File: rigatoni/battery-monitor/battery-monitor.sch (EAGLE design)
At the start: 39 parts, among them J1 S2B-XH-A_(LF)(SN), J2 QSH-030-01-X-D-A-XX, J4 S4B-XH-A(LF)(SN), Q1 STT4P3LLH6, U1 LT1930ES5TRMPBF_BOOST_CONV, U2 NUCLEO-H743ZI-HEADER, U3 TPSM84205EAB

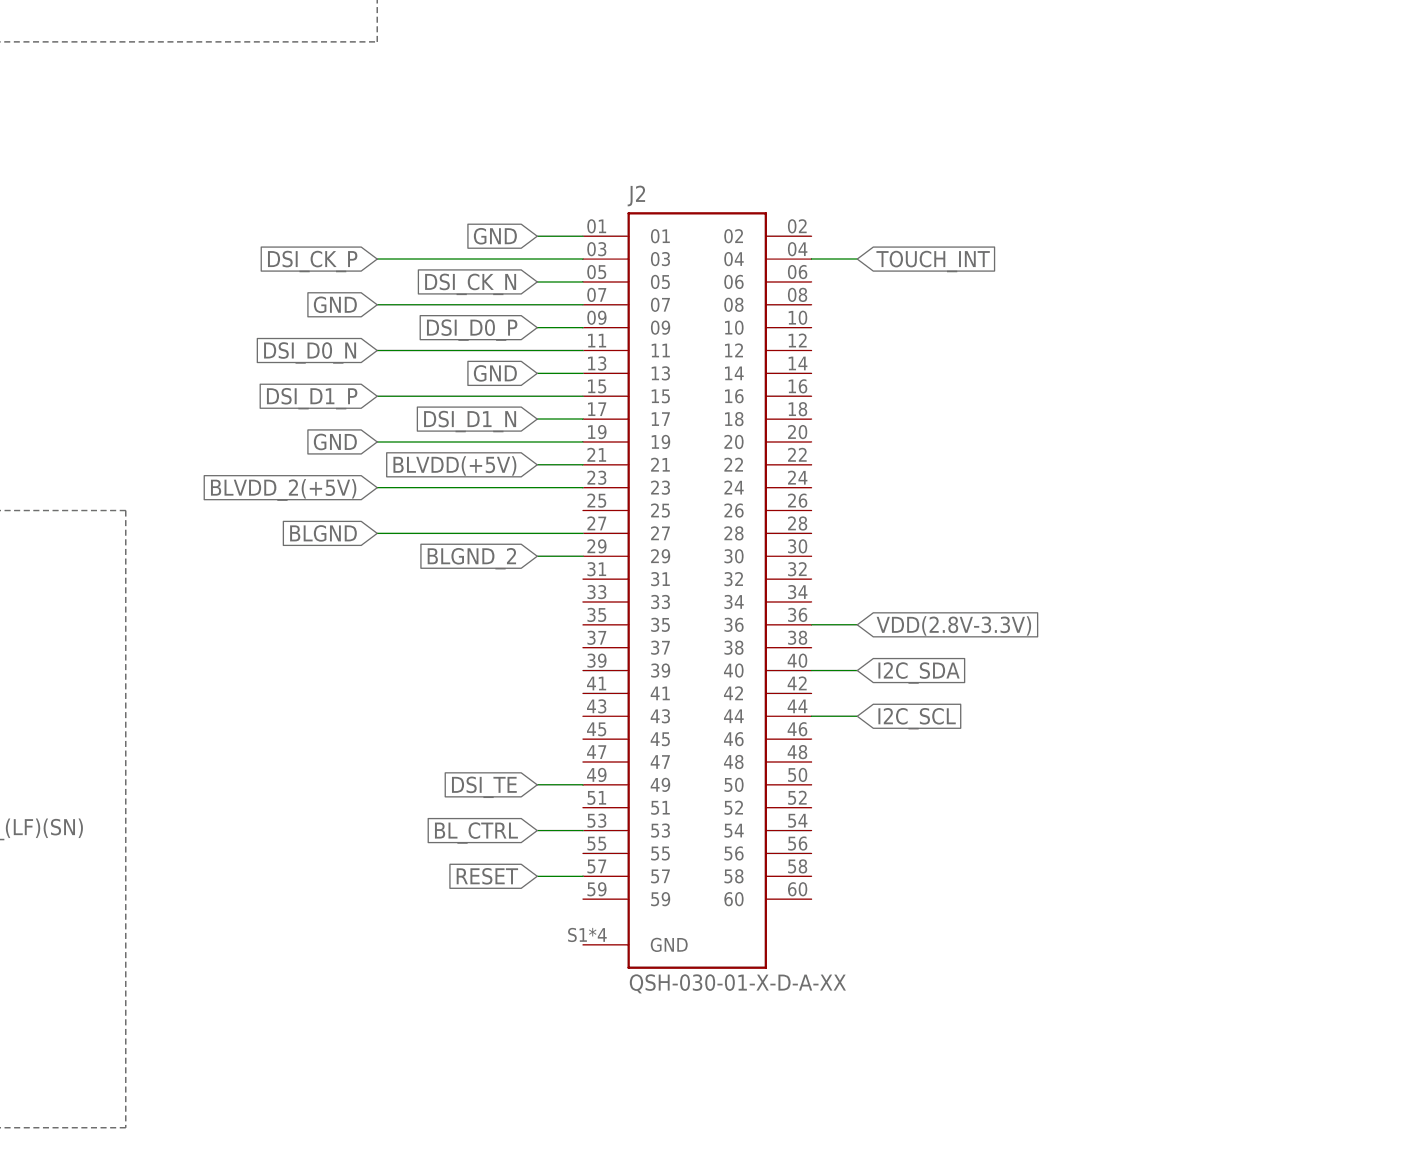
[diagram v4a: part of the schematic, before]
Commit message: Update battery-monitor.sch
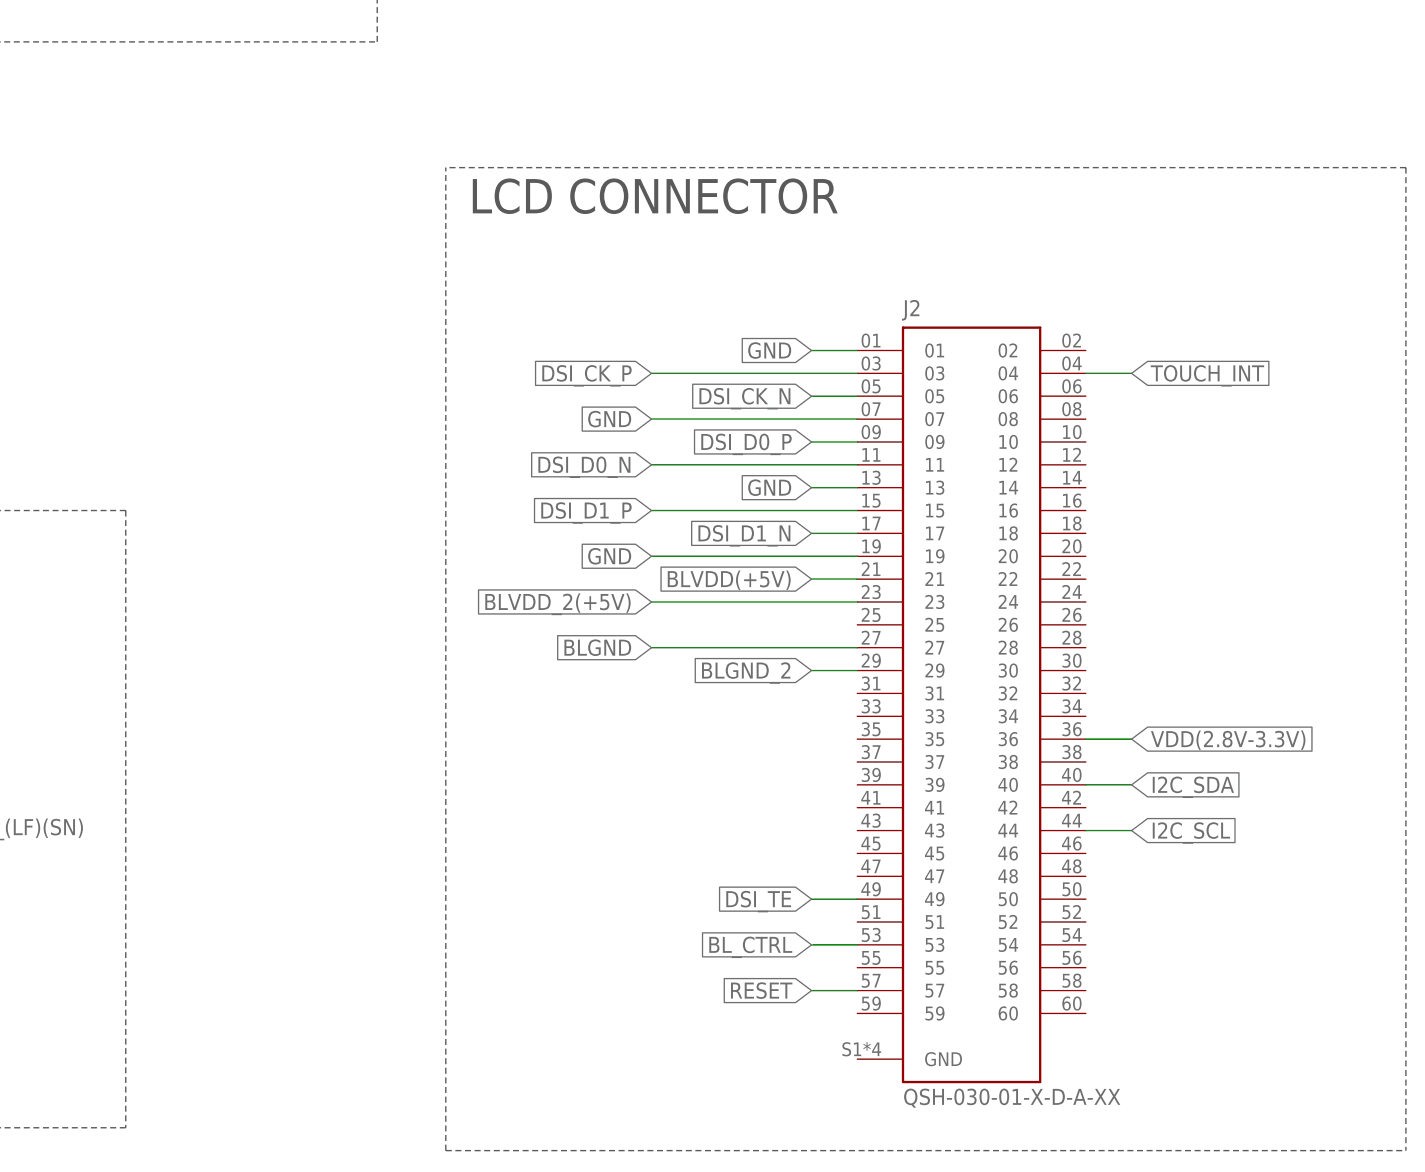
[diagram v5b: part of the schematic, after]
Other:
- note added: "LCD CONNECTOR"
- moved on the sheet: J2
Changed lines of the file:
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@@
 <text x="119.38" y="320.04" size="1.27" layer="97">*Note: C2 should be
 rated @ 25V</text>
+<wire x1="487.68" y1="119.38" x2="381" y2="119.38" width="0.1524" layer="97" style="longdash"/>
+<wire x1="487.68" y1="119.38" x2="487.68" y2="10.16" width="0.1524" layer="97" style="longdash"/>
+<wire x1="381" y1="10.16" x2="487.68" y2="10.16" width="0.1524" layer="97" style="longdash"/>
+<wire x1="381" y1="10.16" x2="381" y2="119.38" width="0.1524" layer="97" style="longdash"/>
+<text x="383.54" y="114.3" size="3.81" layer="97" font="vector">LCD CONNECTOR</text>
 </plain>
 <instances>
@@
 <attribute name="VALUE" x="292.1" y="156.21" size="1.778" layer="96" rot="MR180"/>
 </instance>
-<instance part="J2" gate="G$1" x="408.94" y="73.66" smashed="yes">
-<attribute name="NAME" x="401.32" y="115.57" size="1.778" layer="95"/>
-<attribute name="VALUE" x="401.32" y="27.94" size="1.778" layer="96"/>
+<instance part="J2" gate="G$1" x="439.42" y="60.96" smashed="yes">
+<attribute name="NAME" x="431.8" y="102.87" size="1.778" layer="95"/>
+<attribute name="VALUE" x="431.8" y="15.24" size="1.778" layer="96"/>
 </instance>
 <instance part="SUPPLY2" gate="G$1" x="60.96" y="256.54" smashed="yes">
@@
 <segment>
 <pinref part="J2" gate="G$1" pin="01"/>
-<wire x1="396.24" y1="111.76" x2="391.16" y2="111.76" width="0.1524" layer="91"/>
-<label x="391.16" y="111.76" size="1.778" layer="95" rot="R180" xref="yes"/>
+<wire x1="426.72" y1="99.06" x2="421.64" y2="99.06" width="0.1524" layer="91"/>
+<label x="421.64" y="99.06" size="1.778" layer="95" rot="R180" xref="yes"/>
 </segment>
 <segment>
 <pinref part="J2" gate="G$1" pin="07"/>
-<wire x1="396.24" y1="104.14" x2="373.38" y2="104.14" width="0.1524" layer="91"/>
-<label x="373.38" y="104.14" size="1.778" layer="95" rot="R180" xref="yes"/>
+<wire x1="426.72" y1="91.44" x2="403.86" y2="91.44" width="0.1524" layer="91"/>
+<label x="403.86" y="91.44" size="1.778" layer="95" rot="R180" xref="yes"/>
 </segment>
 <segment>
 <pinref part="J2" gate="G$1" pin="13"/>
-<wire x1="396.24" y1="96.52" x2="391.16" y2="96.52" width="0.1524" layer="91"/>
-<label x="391.16" y="96.52" size="1.778" layer="95" rot="R180" xref="yes"/>
+<wire x1="426.72" y1="83.82" x2="421.64" y2="83.82" width="0.1524" layer="91"/>
+<label x="421.64" y="83.82" size="1.778" layer="95" rot="R180" xref="yes"/>
 </segment>
 <segment>
 <pinref part="J2" gate="G$1" pin="19"/>
-<wire x1="396.24" y1="88.9" x2="373.38" y2="88.9" width="0.1524" layer="91"/>
-<label x="373.38" y="88.9" size="1.778" layer="95" rot="R180" xref="yes"/>
+<wire x1="426.72" y1="76.2" x2="403.86" y2="76.2" width="0.1524" layer="91"/>
+<label x="403.86" y="76.2" size="1.778" layer="95" rot="R180" xref="yes"/>
 </segment>
 <segment>
@@
 <segment>
 <pinref part="J2" gate="G$1" pin="03"/>
-<wire x1="396.24" y1="109.22" x2="373.38" y2="109.22" width="0.1524" layer="91"/>
-<label x="373.38" y="109.22" size="1.778" layer="95" rot="R180" xref="yes"/>
+<wire x1="426.72" y1="96.52" x2="403.86" y2="96.52" width="0.1524" layer="91"/>
+<label x="403.86" y="96.52" size="1.778" layer="95" rot="R180" xref="yes"/>
 </segment>
 <segment>
@@
 <segment>
 <pinref part="J2" gate="G$1" pin="04"/>
-<wire x1="421.64" y1="109.22" x2="426.72" y2="109.22" width="0.1524" layer="91"/>
-<label x="426.72" y="109.22" size="1.778" layer="95" xref="yes"/>
+<wire x1="452.12" y1="96.52" x2="457.2" y2="96.52" width="0.1524" layer="91"/>
+<label x="457.2" y="96.52" size="1.778" layer="95" xref="yes"/>
 </segment>
 </net>
@@
 <segment>
 <pinref part="J2" gate="G$1" pin="05"/>
-<wire x1="396.24" y1="106.68" x2="391.16" y2="106.68" width="0.1524" layer="91"/>
-<label x="391.16" y="106.68" size="1.778" layer="95" rot="R180" xref="yes"/>
+<wire x1="426.72" y1="93.98" x2="421.64" y2="93.98" width="0.1524" layer="91"/>
+<label x="421.64" y="93.98" size="1.778" layer="95" rot="R180" xref="yes"/>
 </segment>
 <segment>
@@
 <segment>
 <pinref part="J2" gate="G$1" pin="09"/>
-<wire x1="396.24" y1="101.6" x2="391.16" y2="101.6" width="0.1524" layer="91"/>
-<label x="391.16" y="101.6" size="1.778" layer="95" rot="R180" xref="yes"/>
+<wire x1="426.72" y1="88.9" x2="421.64" y2="88.9" width="0.1524" layer="91"/>
+<label x="421.64" y="88.9" size="1.778" layer="95" rot="R180" xref="yes"/>
 </segment>
 <segment>
@@
 <segment>
 <pinref part="J2" gate="G$1" pin="11"/>
-<wire x1="396.24" y1="99.06" x2="373.38" y2="99.06" width="0.1524" layer="91"/>
-<label x="373.38" y="99.06" size="1.778" layer="95" rot="R180" xref="yes"/>
+<wire x1="426.72" y1="86.36" x2="403.86" y2="86.36" width="0.1524" layer="91"/>
+<label x="403.86" y="86.36" size="1.778" layer="95" rot="R180" xref="yes"/>
 </segment>
 <segment>
@@
 <segment>
 <pinref part="J2" gate="G$1" pin="15"/>
-<wire x1="396.24" y1="93.98" x2="373.38" y2="93.98" width="0.1524" layer="91"/>
-<label x="373.38" y="93.98" size="1.778" layer="95" rot="R180" xref="yes"/>
+<wire x1="426.72" y1="81.28" x2="403.86" y2="81.28" width="0.1524" layer="91"/>
+<label x="403.86" y="81.28" size="1.778" layer="95" rot="R180" xref="yes"/>
 </segment>
 <segment>
@@
 <segment>
 <pinref part="J2" gate="G$1" pin="17"/>
-<wire x1="396.24" y1="91.44" x2="391.16" y2="91.44" width="0.1524" layer="91"/>
-<label x="391.16" y="91.44" size="1.778" layer="95" rot="R180" xref="yes"/>
+<wire x1="426.72" y1="78.74" x2="421.64" y2="78.74" width="0.1524" layer="91"/>
+<label x="421.64" y="78.74" size="1.778" layer="95" rot="R180" xref="yes"/>
 </segment>
 <segment>
@@
 <segment>
 <pinref part="J2" gate="G$1" pin="21"/>
-<wire x1="396.24" y1="86.36" x2="391.16" y2="86.36" width="0.1524" layer="91"/>
-<label x="391.16" y="86.36" size="1.778" layer="95" rot="R180" xref="yes"/>
+<wire x1="426.72" y1="73.66" x2="421.64" y2="73.66" width="0.1524" layer="91"/>
+<label x="421.64" y="73.66" size="1.778" layer="95" rot="R180" xref="yes"/>
 </segment>
 </net>
@@
 <segment>
 <pinref part="J2" gate="G$1" pin="23"/>
-<wire x1="396.24" y1="83.82" x2="373.38" y2="83.82" width="0.1524" layer="91"/>
-<label x="373.38" y="83.82" size="1.778" layer="95" rot="R180" xref="yes"/>
+<wire x1="426.72" y1="71.12" x2="403.86" y2="71.12" width="0.1524" layer="91"/>
+<label x="403.86" y="71.12" size="1.778" layer="95" rot="R180" xref="yes"/>
 </segment>
 </net>
@@
 <segment>
 <pinref part="J2" gate="G$1" pin="27"/>
-<wire x1="396.24" y1="78.74" x2="373.38" y2="78.74" width="0.1524" layer="91"/>
-<label x="373.38" y="78.74" size="1.778" layer="95" rot="R180" xref="yes"/>
+<wire x1="426.72" y1="66.04" x2="403.86" y2="66.04" width="0.1524" layer="91"/>
+<label x="403.86" y="66.04" size="1.778" layer="95" rot="R180" xref="yes"/>
 </segment>
 </net>
@@
 <segment>
 <pinref part="J2" gate="G$1" pin="29"/>
-<wire x1="396.24" y1="76.2" x2="391.16" y2="76.2" width="0.1524" layer="91"/>
-<label x="391.16" y="76.2" size="1.778" layer="95" rot="R180" xref="yes"/>
+<wire x1="426.72" y1="63.5" x2="421.64" y2="63.5" width="0.1524" layer="91"/>
+<label x="421.64" y="63.5" size="1.778" layer="95" rot="R180" xref="yes"/>
 </segment>
 </net>
@@
 <segment>
 <pinref part="J2" gate="G$1" pin="36"/>
-<wire x1="421.64" y1="68.58" x2="426.72" y2="68.58" width="0.1524" layer="91"/>
-<label x="426.72" y="68.58" size="1.778" layer="95" xref="yes"/>
+<wire x1="452.12" y1="55.88" x2="457.2" y2="55.88" width="0.1524" layer="91"/>
+<label x="457.2" y="55.88" size="1.778" layer="95" xref="yes"/>
 </segment>
 </net>
@@
 <segment>
 <pinref part="J2" gate="G$1" pin="40"/>
-<wire x1="421.64" y1="63.5" x2="426.72" y2="63.5" width="0.1524" layer="91"/>
-<label x="426.72" y="63.5" size="1.778" layer="95" xref="yes"/>
+<wire x1="452.12" y1="50.8" x2="457.2" y2="50.8" width="0.1524" layer="91"/>
+<label x="457.2" y="50.8" size="1.778" layer="95" xref="yes"/>
 </segment>
 </net>
@@
 <segment>
 <pinref part="J2" gate="G$1" pin="44"/>
-<wire x1="421.64" y1="58.42" x2="426.72" y2="58.42" width="0.1524" layer="91"/>
-<label x="426.72" y="58.42" size="1.778" layer="95" xref="yes"/>
+<wire x1="452.12" y1="45.72" x2="457.2" y2="45.72" width="0.1524" layer="91"/>
+<label x="457.2" y="45.72" size="1.778" layer="95" xref="yes"/>
 </segment>
 </net>
@@
 <segment>
 <pinref part="J2" gate="G$1" pin="49"/>
-<wire x1="396.24" y1="50.8" x2="391.16" y2="50.8" width="0.1524" layer="91"/>
-<label x="391.16" y="50.8" size="1.778" layer="95" rot="R180" xref="yes"/>
+<wire x1="426.72" y1="38.1" x2="421.64" y2="38.1" width="0.1524" layer="91"/>
+<label x="421.64" y="38.1" size="1.778" layer="95" rot="R180" xref="yes"/>
 </segment>
 </net>
@@
 <segment>
 <pinref part="J2" gate="G$1" pin="53"/>
-<wire x1="396.24" y1="45.72" x2="391.16" y2="45.72" width="0.1524" layer="91"/>
-<label x="391.16" y="45.72" size="1.778" layer="95" rot="R180" xref="yes"/>
+<wire x1="426.72" y1="33.02" x2="421.64" y2="33.02" width="0.1524" layer="91"/>
+<label x="421.64" y="33.02" size="1.778" layer="95" rot="R180" xref="yes"/>
 </segment>
 </net>
@@
 <segment>
 <pinref part="J2" gate="G$1" pin="57"/>
-<wire x1="396.24" y1="40.64" x2="391.16" y2="40.64" width="0.1524" layer="91"/>
-<label x="391.16" y="40.64" size="1.778" layer="95" rot="R180" xref="yes"/>
-</segment>
-</net>
+<wire x1="426.72" y1="27.94" x2="421.64" y2="27.94" width="0.1524" layer="91"/>
+<label x="421.64" y="27.94" size="1.778" layer="95" rot="R180" xref="yes"/>
+</segment>
+</net>

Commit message: Finished Rough Draft for Schematic Review
Not updated with changes suggested during schematic review
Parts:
- removed J2: QSH-030-01-X-D-A-XX, QSH-030-01-X-D-A-XX:QSH-030-01-X-D-A-XX
- added J5: S2B-XH-A_(LF)(SN), drive_brake:S2B-XH-A_(LF)(SN)
- added J6: S4B-XH-A(LF)(SN), drive_brake:S4B-XH-A(LF)(SN)
- added JP1, JP2: (no value), SparkFun:M06SIP
- added Q2, Q3, Q4, Q5: BSS138, SparkFun:MOSFET-NCHANNELSMD
- added R10, R11, R14, R15, R16, R17, R18, R7: 10K, SparkFun:RESISTOR0603-RES
- added R19: 1k, rcl:R-US_R0603
- added R6: 220 Ω, rcl:R-US_R0603
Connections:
- removed net BLGND: J2.27
- removed net BLGND_2: J2.29
- removed net BLVDD(+5V): J2.21
- removed net BLVDD_2(+5V): J2.23
- removed net BL_CTRL: J2.53
- removed net DSI_CK_N: J2.05, U2G$6.D5/TIMER_A_PWM2
- removed net DSI_CK_P: J2.03, U2G$6.D6/TIMER_A_PWM1
- removed net DSI_D0_N: J2.11, U2G$6.D2/IO
- removed net DSI_D0_P: J2.09, U2G$5.D8/IO
- removed net DSI_D1_N: J2.17, U2G$6.D7/IO
- removed net DSI_D1_P: J2.15, U2G$6.D4/IO
- removed net DSI_TE: J2.49
- removed net N$10: D5.C, Q1.D
- removed net N$11: D6.A, F2.2
- removed net RESET: J2.57
- removed net TOUCH_INT: J2.04
- removed net VDD(2.8V-3.3V): J2.36
- new net HV: JP2.3, R10.1, R14.1, R16.1, R18.1
- new net HV1: JP2.1, Q3.D, R14.2
- new net HV2: JP2.2, Q4.D, R16.2
- new net HV3: JP2.5, Q5.D, R18.2
- new net HV4: JP2.6, Q2.D, R10.2
- new net LED: R6.1, U2G$4.D64/IO
- new net LV: JP1.4, Q2.G, Q3.G, Q4.G, Q5.G, R11.1, R15.1, R17.1, R7.1
- new net LV1: JP1.6, Q3.S, R11.2
- new net LV2: JP1.5, Q4.S, R15.2
- new net LV3: JP1.2, Q5.S, R17.2
- new net LV4: JP1.1, Q2.S, R7.2
- new net N$9: J5.1, R6.2
- net +5V: now also D6.A, F2.2, J6.3
- net GND: now also J5.2, J6.4, JP1.3, JP2.4; no longer J2.01, J2.07, J2.13, J2.19
- net I2C_SCL: now also J6.1, U2G$5.D15/I2C_A_SCL; no longer J2.44
- net I2C_SDA: now also J6.2, U2G$5.D14/I2C_A_SDA; no longer J2.40
- net N$2: now also D5.C, Q1.D, R19.1
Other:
- note added: "High Voltage"
- note added: "I2C LEVEL SHIFTER"
- note added: "LED CONNECTOR"
- note added: "Low Voltage"
- moved on the sheet: C1, C10, C11, C18, C2, C3, C4, C7, C8, C9, D1, D2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

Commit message: Implemented changes from schematic review
LED Connector and Power Circuitry still needs to be updated in schematic
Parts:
- removed JP1, JP2: (no value), SparkFun:M06SIP
- removed Q2, Q3, Q4, Q5: BSS138, SparkFun:MOSFET-NCHANNELSMD
- removed R10, R11, R14, R15, R16, R17, R18, R7: 10K, SparkFun:RESISTOR0603-RES
- removed R19: 1k, rcl:R-US_R0603
- C1: value 1 uF -> 47 uF
- R1: value 5 kΩ -> 20 kΩ
- R3: value 55 kΩ -> 350 kΩ
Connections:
- removed net HV: JP2.3, R10.1, R14.1, R16.1, R18.1
- removed net HV1: JP2.1, Q3.D, R14.2
- removed net HV2: JP2.2, Q4.D, R16.2
- removed net HV3: JP2.5, Q5.D, R18.2
- removed net HV4: JP2.6, Q2.D, R10.2
- removed net LV: JP1.4, Q2.G, Q3.G, Q4.G, Q5.G, R11.1, R15.1, R17.1, R7.1
- removed net LV1: JP1.6, Q3.S, R11.2
- removed net LV2: JP1.5, Q4.S, R15.2
- removed net LV3: JP1.2, Q5.S, R17.2
- removed net LV4: JP1.1, Q2.S, R7.2
- net GND: now also U2G$4.GND_CN9, U2G$5.GND_CN7; no longer JP1.3, JP2.4
- net N$2: no longer R19.1
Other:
- note added: "LED CONNECTOR (UNDER CONSTRUCTION)"
- note removed: "High Voltage"
- note removed: "I2C LEVEL SHIFTER"
- note removed: "LED CONNECTOR"
- note removed: "Low Voltage"
- moved on the sheet: J5, R6

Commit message: Started routing the board
LED connector still not completed
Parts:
- removed Q1: STT4P3LLH6, RoboJackets-Discrete:STT4P3LLH6
- added CR1: LSM115JE3/TR13, RoboRacing_STM:LSM115JE3/TR13
- added R10: 50kΩ, SparkFun:RESISTOR0603-RES
- added R11: 100kΩ, SparkFun:RESISTOR0603-RES
- added R7: 150R, rcl:R-US_R0603
- C4: value 100uF -> 47uF
- R5: value 1k -> 500R
- renumbered J3 to J2
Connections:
- removed net N$4 (its old number): C2.1, Q1.S, TVS_1.C, U3.VIN
- new net N$10: D6.C, R7.2
- new net N$7: D5.C, R5.2
- net +5V: no longer C3.1, D6.C
- net 5V_MAIN: now also C3.1
- net CURR_DATA: now also R10.1, R10.2, R11.1
- net GND: now also R11.2, R7.1, U2G$2.GND_CN12, U2G$3.GND_CN8, U2G$6.GND_CN10
- net N$2: now also CR1.2; no longer D5.C, Q1.D
- net N$3: now also C2.1, CR1.1, TVS_1.C, U3.VIN; no longer Q1.G, R5.2
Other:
- note added: "BATTERY VOLTAGE DIVIDER"
- note added: "resistor network (R10, R11, R12, R13) shifts up voltage output from -5V:5V to 0V:3.3V (capacitor for smoothing)"
- note removed: "VOLTAGE DIVIDER"
- note removed: "resistor network (R12 and R13) shifts up voltage output from -5V:5V to 0V:5V (capacitor for smoothing)"
- moved on the sheet: C18, C3, D5, D6, F2, J4, J5, R12, R13, R5, R6
